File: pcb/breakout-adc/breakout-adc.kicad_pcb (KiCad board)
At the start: 4 copper layers, 100 x 62 mm, 104 parts, among them J1 Screw_Terminal_01x04, J10 Conn_01x01_Pin, J11 Conn_01x12_Pin, J12 Conn_01x12_Pin, J13 Conn_01x01_Pin, J14 Conn_01x01_Pin, J15 FX18-120P-0.8SV20, J2 Screw_Terminal_01x02, J20 Conn_02x02_Counter_Clockwise, J21 Conn_02x04_Odd_Even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

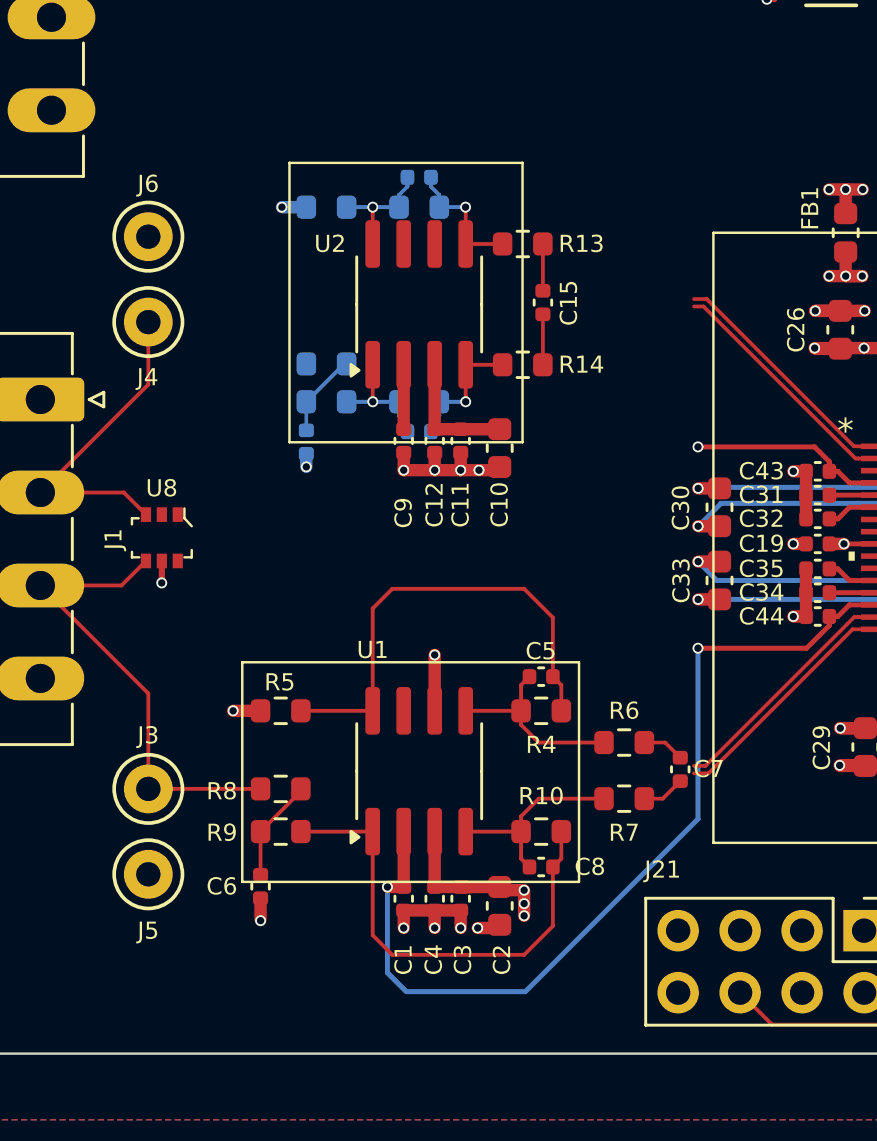
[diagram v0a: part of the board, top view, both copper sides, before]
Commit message: [adc][pcb] cleanup upper op amp silks pre copy
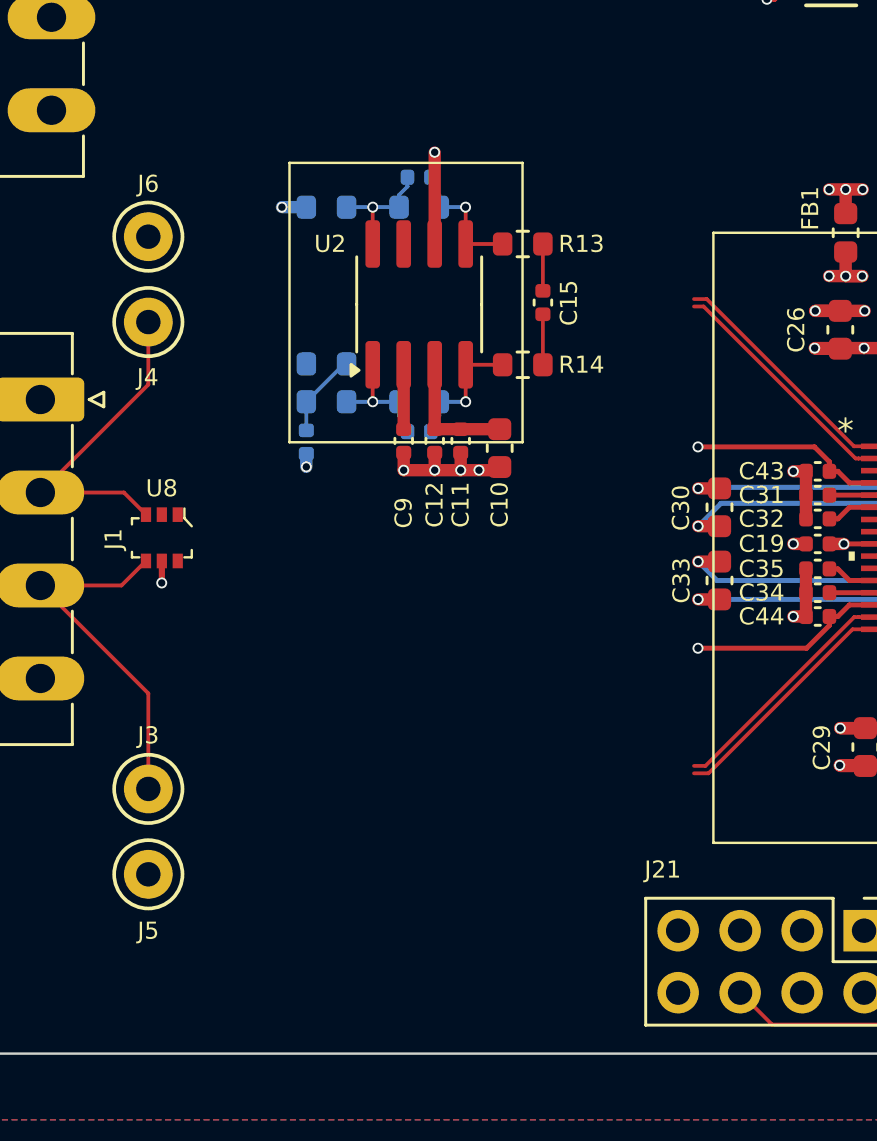
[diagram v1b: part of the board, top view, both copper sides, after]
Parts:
- removed C1: 0.1uf, Capacitor_SMD:C_0402_1005Metric
- removed C2: 10uf, Capacitor_SMD:C_0603_1608Metric
- removed C3, C4: 0.01uf, Capacitor_SMD:C_0402_1005Metric
- removed C5, C8: 330pf, Capacitor_SMD:C_0402_1005Metric
- removed C6, C7: 160pf, Capacitor_SMD:C_0402_1005Metric
- removed R10, R4, R6, R7: 270, Resistor_SMD:R_0603_1608Metric
- removed R5: 2.4k, Resistor_SMD:R_0603_1608Metric
- removed R8, R9: 1.2K, Resistor_SMD:R_0603_1608Metric
- removed U1: LMH6551MA, Package_SO:SOIC-8_3.9x4.9mm_P1.27mm
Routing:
- net X_VCM: track 37.8 -> 8.41 mm, vias 2 -> 1
- net Net-(C8-Pad2): track 19.4 -> 0.00 mm
- net Net-(C5-Pad1): track 19.3 -> 0.00 mm
- net Net-(C8-Pad1): track 8.19 -> 0.00 mm
- net Net-(C5-Pad2): track 8.09 -> 0.00 mm
- net +3V3ADC: track 49.9 -> 42.2 mm, vias 19 -> 16
- net GND: track 55.1 -> 49.1 mm, vias 44 -> 38
- net /X: track 19.5 -> 14.9 mm
- net Net-(C6-Pad2): track 4.30 -> 0.00 mm
- net /adc/X_N: track 12.0 -> 10.0 mm
- net /adc/X_P: track 11.7 -> 9.95 mm

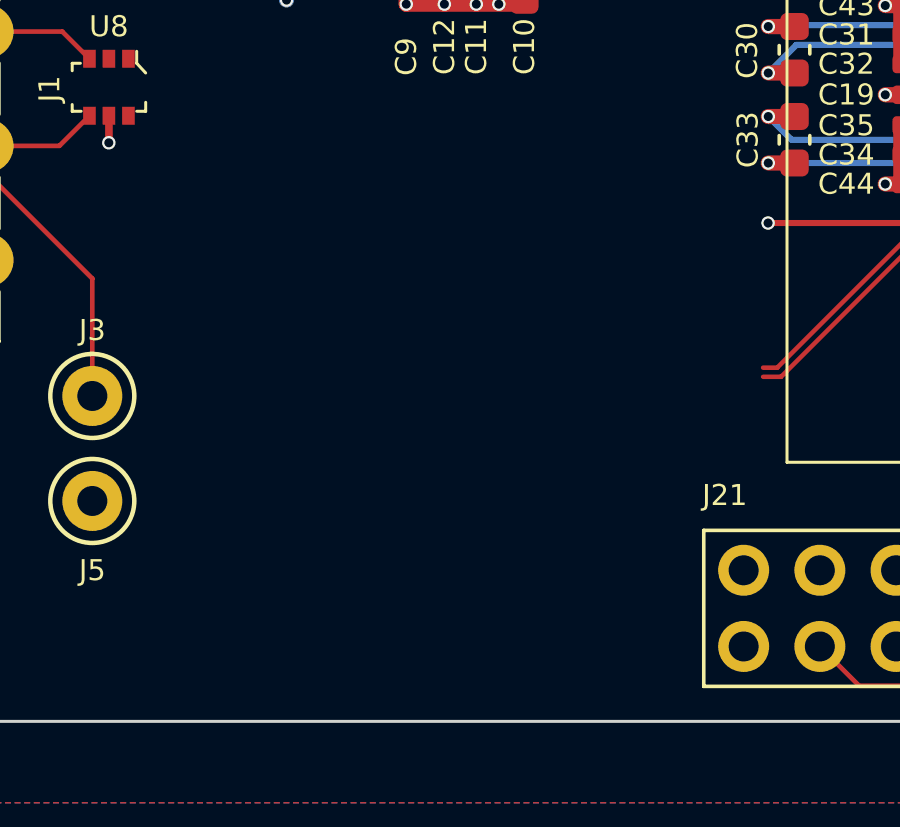
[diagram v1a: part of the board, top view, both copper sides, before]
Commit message: [adc][pcb] redo lower op amp to match the upper
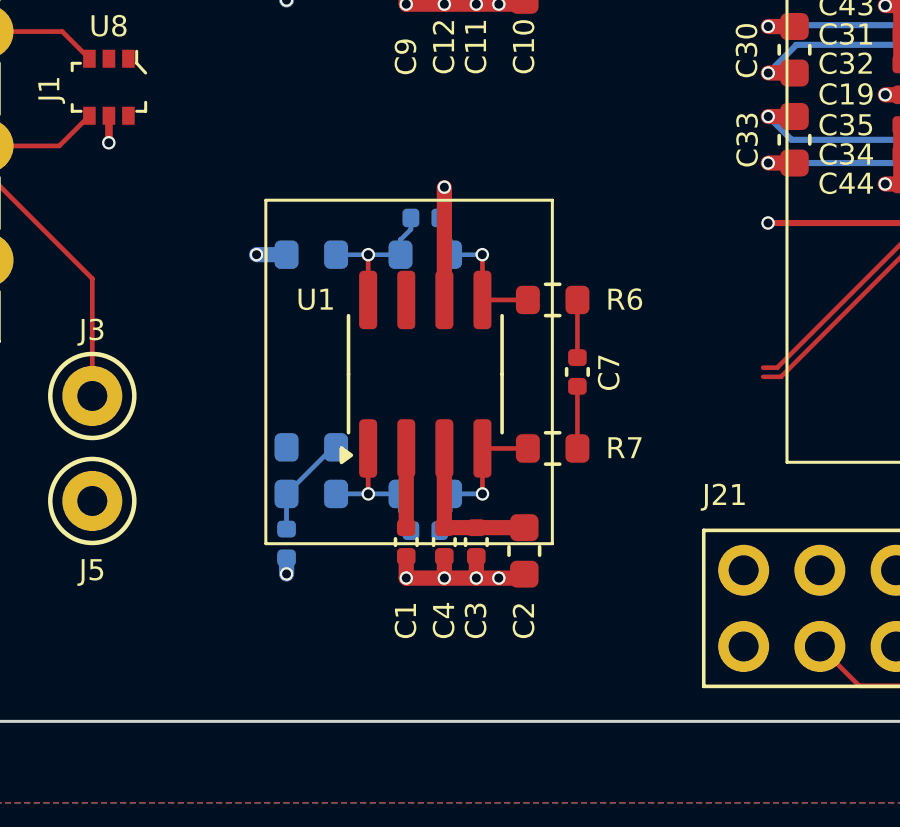
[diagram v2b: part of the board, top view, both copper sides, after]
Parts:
- added C1: 0.1uf, Capacitor_SMD:C_0402_1005Metric, F.Cu at (131.8, 99.6)
- added C2: 10uf, Capacitor_SMD:C_0603_1608Metric, F.Cu at (135.7, 99.9)
- added C3: 0.01uf, Capacitor_SMD:C_0402_1005Metric, F.Cu at (134.1, 99.6)
- added C4: 0.01uf, Capacitor_SMD:C_0402_1005Metric, F.Cu at (133.0, 99.6)
- added C5: 330pf, Capacitor_SMD:C_0402_1005Metric, B.Cu at (132.4, 88.8)
- added C6: 160pf, Capacitor_SMD:C_0402_1005Metric, B.Cu at (127.8, 99.6)
- added C7: 160pf, Capacitor_SMD:C_0402_1005Metric, F.Cu at (137.5, 93.9)
- added C8: 330pf, Capacitor_SMD:C_0402_1005Metric, B.Cu at (132.4, 99.2)
- added R10: 270, Resistor_SMD:R_0603_1608Metric, B.Cu at (132.4, 98.0)
- added R4: 270, Resistor_SMD:R_0603_1608Metric, B.Cu at (132.4, 90.0)
- added R5: 2.4k, Resistor_SMD:R_0603_1608Metric, B.Cu at (128.6, 90.0)
- added R6: 270, Resistor_SMD:R_0603_1608Metric, F.Cu at (136.6, 91.5)
- added R7: 270, Resistor_SMD:R_0603_1608Metric, F.Cu at (136.6, 96.4)
- added R8: 1.2K, Resistor_SMD:R_0603_1608Metric, B.Cu at (128.6, 96.4)
- added R9: 1.2K, Resistor_SMD:R_0603_1608Metric, B.Cu at (128.6, 98.0)
- added U1: LMH6551MA, Package_SO:SOIC-8_3.9x4.9mm_P1.27mm, F.Cu at (132.4, 94.0)
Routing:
- net GND: track 49.1 -> 60.5 mm, vias 38 -> 45
- net Net-(C8-Pad1): track 0.00 -> 5.48 mm, vias 0 -> 1
- net Net-(C5-Pad2): track 0.00 -> 5.47 mm, vias 0 -> 1
- net +3V3ADC: track 42.2 -> 47.5 mm
- net Net-(C5-Pad1): track 0.00 -> 5.04 mm, vias 0 -> 1
- net Net-(C8-Pad2): track 0.00 -> 5.04 mm, vias 0 -> 1
- net Net-(C6-Pad2): track 0.00 -> 3.46 mm
- net X_VCM: track 8.41 -> 11.0 mm
- net /adc/X_P: track 9.95 -> 12.0 mm
- net /adc/X_N: track 10.0 -> 12.0 mm

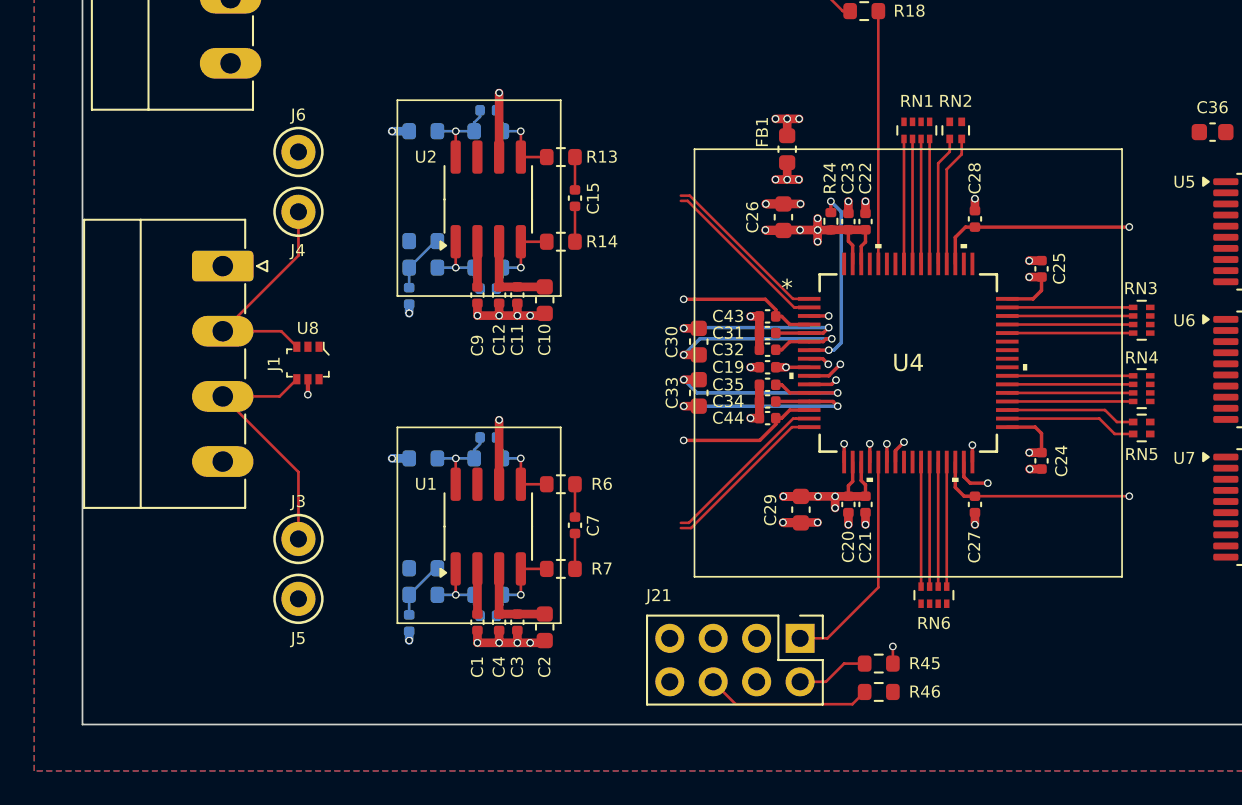
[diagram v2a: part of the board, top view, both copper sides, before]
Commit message: [adc][pcb] op amps fully routed
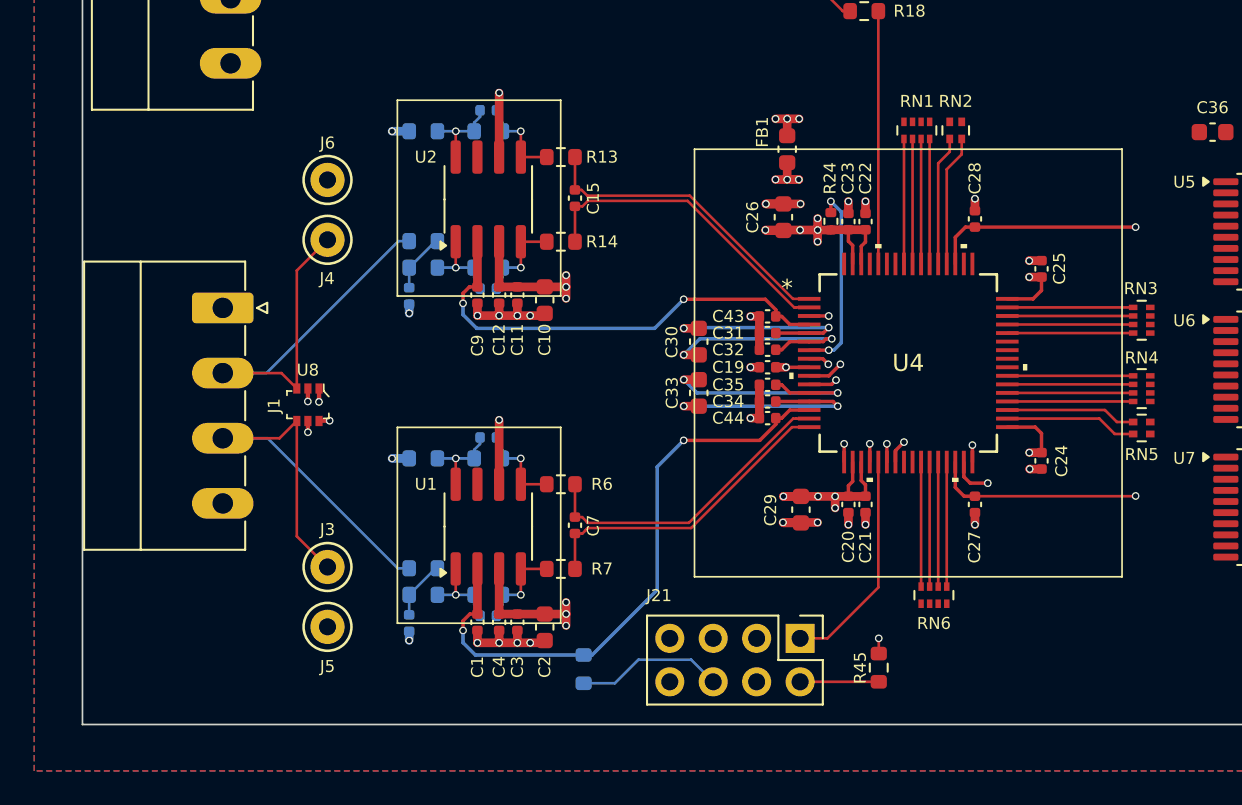
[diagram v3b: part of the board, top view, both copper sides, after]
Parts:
- R46: moved to B.Cu
- moved R46 17.3 mm to (138.0, 102.3), turned to -90 degrees
- moved J1 2.45 mm to (116.9, 81.2)
- moved U8 2.44 mm to (121.9, 86.8)
- moved J3 2.36 mm to (123.0, 96.3)
- moved J5 2.36 mm to (123.0, 99.8)
- moved J4 2.36 mm to (123.0, 77.2)
- moved J6 2.36 mm to (123.0, 73.7)
- moved R45 0.24 mm to (155.2, 102.2), turned to -90 degrees
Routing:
- net X_VCM: track 11.0 -> 35.9 mm, vias 1 -> 2
- net Y_VCM: track 10.8 -> 26.9 mm, vias 1 -> 2
- net /Y: track 13.5 -> 28.2 mm
- net /X: track 14.9 -> 28.1 mm
- net /adc/X_P: track 12.0 -> 18.5 mm
- net /adc/X_N: track 12.0 -> 18.4 mm
- net /adc/Y_N: track 11.9 -> 18.3 mm
- net /adc/Y_P: track 12.2 -> 18.5 mm
- net +3V3ADC: track 47.5 -> 52.6 mm, vias 16 -> 22
- net GND: track 60.5 -> 62.7 mm, vias 45 -> 48
- net Net-(J21-Pin_6): track 9.69 -> 8.68 mm
- net +3V3: track 32.4 -> 33.1 mm

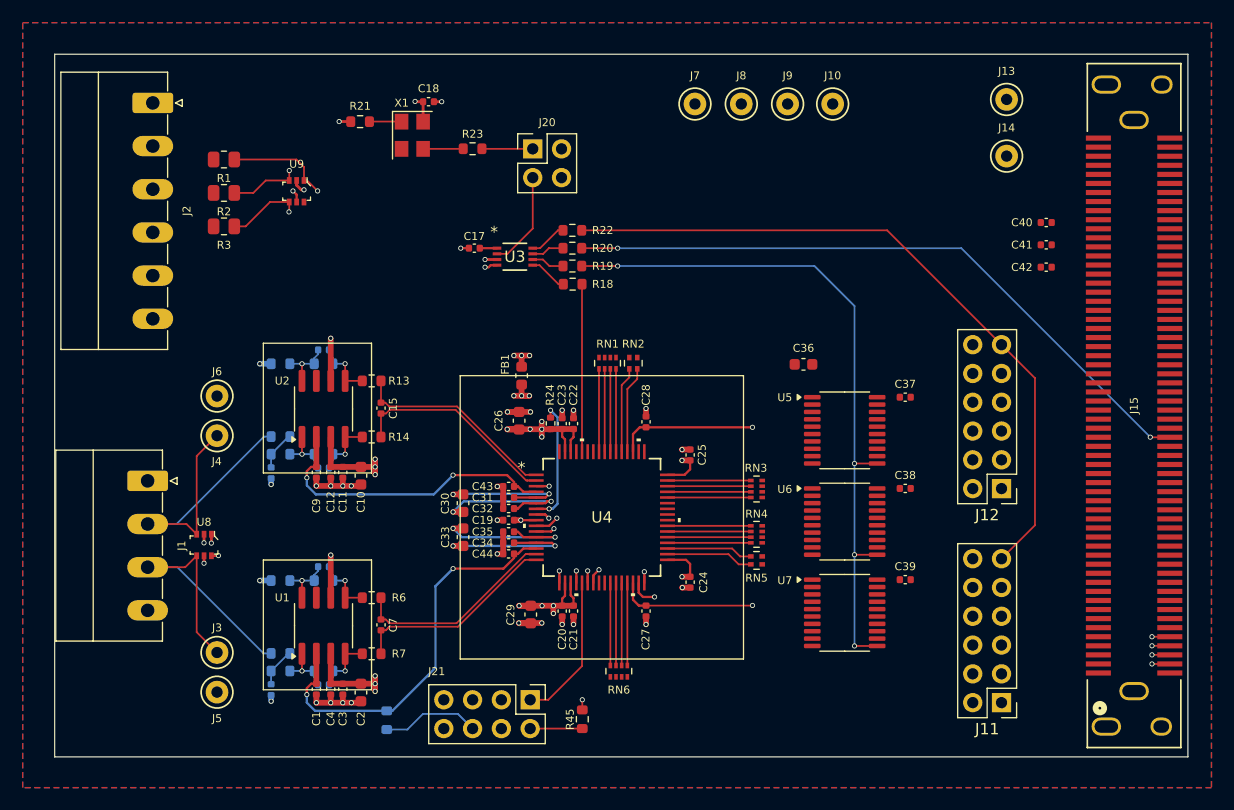
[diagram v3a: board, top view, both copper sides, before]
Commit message: [adc][pcb] rgb esd protection p&r
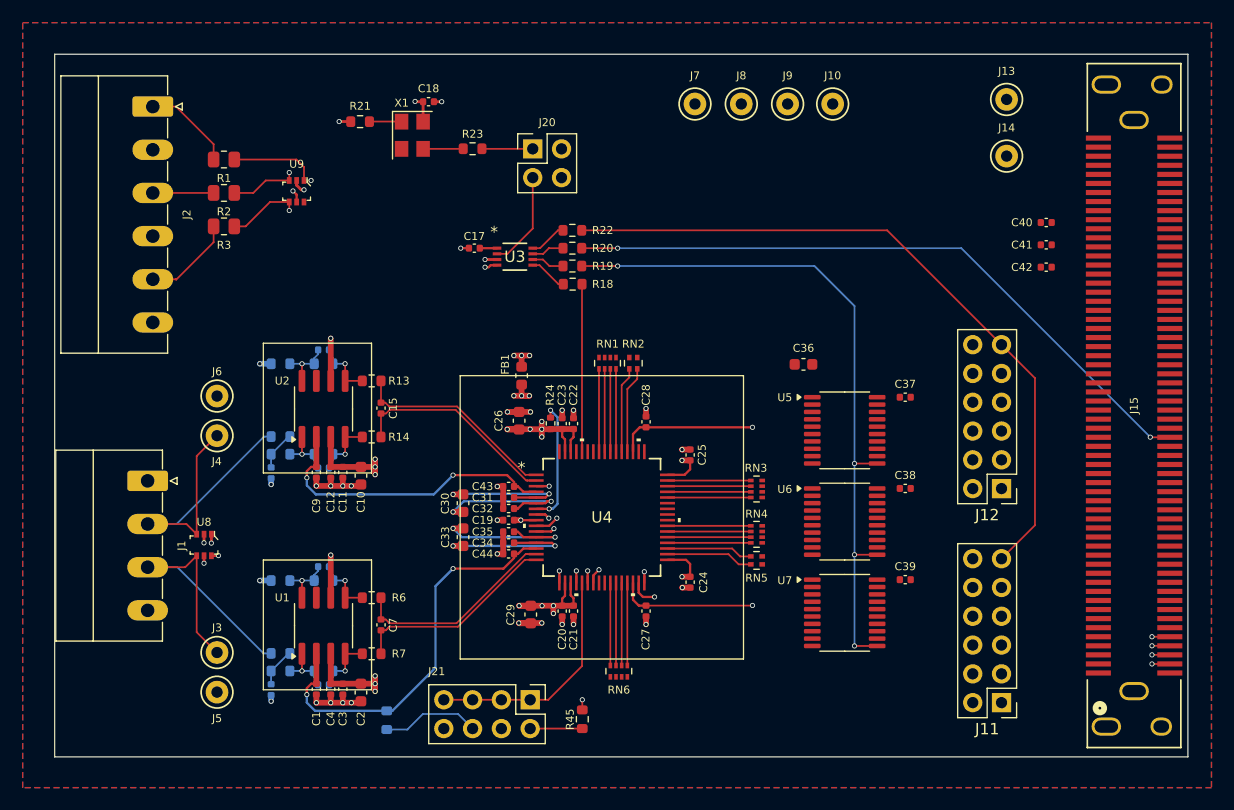
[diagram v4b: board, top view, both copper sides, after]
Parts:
- moved J2 0.33 mm to (117.3, 48.2)
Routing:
- net Net-(J2-Pin_5): track 0.00 -> 8.15 mm
- net Net-(J2-Pin_1): track 0.00 -> 8.09 mm
- net Net-(J21-Pin_1): track 13.1 -> 20.8 mm
- net Net-(J2-Pin_3): track 0.00 -> 5.37 mm
- net /R: track 9.19 -> 8.23 mm
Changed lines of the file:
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@@
 	(footprint "Connector_Phoenix_MC:PhoenixContact_MC_1,5_6-G-3.81_1x06_P3.81mm_Horizontal"
 		(layer "F.Cu")
-		(at 117.3325 47.83 -90)
+		(at 117.3325 48.155 -90)
 		(descr "Generic Phoenix Contact connector footprint for: MC_1,5/6-G-3.81; number of pins: 06; pin pitch: 3.81mm; Angled || order number: 1803316 8A 160V")
 		(tags "phoenix_contact connector MC_01x06_G_3.81mm")
@@
 	)
 	(segment
-		(start 130.95 54.675)
-		(end 131.875 55.6)
+		(start 131.3 54.675)
+		(end 130.675 54.675)
 		(width 0.156464)
 		(layer "F.Cu")
@@
 		(net 23)
 	)
-	(segment
-		(start 130.675 54.675)
-		(end 130.95 54.675)
-		(width 0.156464)
-		(layer "F.Cu")
-		(net 23)
-	)
 	(via
-		(at 131.875 55.6)
+		(at 131.3 54.675)
 		(size 0.45)
 		(drill 0.3)
@@
 	(segment
 		(start 129.375 54.675)
-		(end 129.375 53.8)
+		(end 129.375 53.975)
 		(width 0.156464)
 		(layer "F.Cu")
@@
 	)
 	(via
-		(at 129.375 53.8)
+		(at 129.375 53.975)
 		(size 0.45)
 		(drill 0.3)
@@
 	)
 	(segment
-		(start 129.375 56.575)
-		(end 129.375 57.425)
-		(width 0.156464)
-		(layer "F.Cu")
-		(net 25)
-	)
-	(segment
 		(start 124.525 58.725)
 		(end 125.525 58.725)
@@
 	)
 	(segment
-		(start 129.375 57.425)
-		(end 129.35 57.45)
+		(start 129.375 57.325)
+		(end 129.375 56.575)
 		(width 0.156464)
 		(layer "F.Cu")
@@
 	)
 	(via
-		(at 129.35 57.45)
+		(at 129.375 57.325)
 		(size 0.45)
 		(drill 0.3)
@@
 	)
 	(segment
+		(start 117.3325 55.775)
+		(end 122.7 55.775)
+		(width 0.156464)
+		(layer "F.Cu")
+		(net 28)
+	)
+	(segment
+		(start 119.38 48.155)
+		(end 122.7 51.475)
+		(width 0.156464)
+		(layer "F.Cu")
+		(net 29)
+	)
+	(segment
+		(start 122.7 51.475)
+		(end 122.7 52.825)
+		(width 0.156464)
+		(layer "F.Cu")
+		(net 29)
+	)
+	(segment
+		(start 117.3325 48.155)
+		(end 119.38 48.155)
+		(width 0.156464)
+		(layer "F.Cu")
+		(net 29)
+	)
+	(segment
+		(start 117.3325 63.395)
+		(end 119.37 63.395)
+		(width 0.156464)
+		(layer "F.Cu")
+		(net 30)
+	)
+	(segment
+		(start 122.7 60.125)
+		(end 122.7 58.725)
+		(width 0.156464)
+		(layer "F.Cu")
+		(net 30)
+	)
+	(segment
+		(start 119.37 63.395)
+		(end 119.4 63.425)
+		(width 0.156464)
+		(layer "F.Cu")
+		(net 30)
+	)
+	(segment
+		(start 119.4 63.425)
+		(end 122.7 60.125)
+		(width 0.156464)
+		(layer "F.Cu")
+		(net 30)
+	)
+	(segment
 		(start 192.225 69.165)
 		(end 195.175 72.115)
@@
 		(width 0.156464)
 		(layer "F.Cu")
+		(net 128)
+	)
+	(segment
+		(start 143.011666 100.5)
+		(end 150.631666 100.5)
+		(width 0.156464)
+		(layer "F.Cu")
